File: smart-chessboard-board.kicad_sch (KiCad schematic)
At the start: 5 parts, among them J101 Conn_01x12_MountingPin

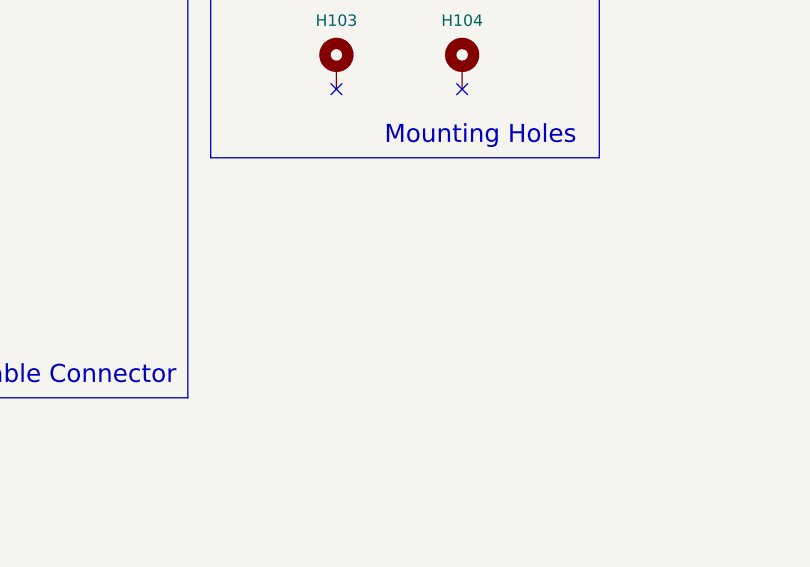
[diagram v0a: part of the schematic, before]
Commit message: complete trace and add test points
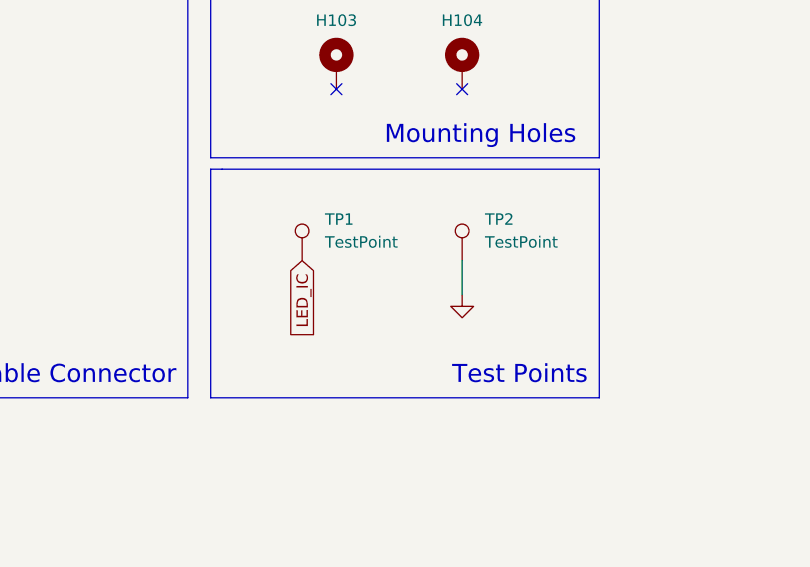
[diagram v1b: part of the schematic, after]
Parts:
- added TP1, TP2: TestPoint, TestPoint:TestPoint_Pad_D2.0mm, symbol Connector:TestPoint
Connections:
- net GND: now also TP2.1
- net LED_IC: now also TP1.1
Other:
- note added: "Test Points"
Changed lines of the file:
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@@
+    (stroke (width 0) (type default) (color 0 0 0 0))
+  )
+  (polyline (pts (xy 100.33 54.61) (xy 101.6 54.61))
     (stroke (width 0) (type default) (color 0 0 0 0))
   )
@@
     (stroke (width 0) (type default) (color 0 0 0 0))
   )
+  (wire (pts (xy 128.27 68.58) (xy 128.27 64.77))
+    (stroke (width 0) (type default) (color 0 0 0 0))
+  )
   (polyline (pts (xy 21.59 20.32) (xy 97.79 20.32))
     (stroke (width 0) (type default) (color 0 0 0 0))
@@
     (stroke (width 0) (type default) (color 0 0 0 0))
   )
+  (polyline (pts (xy 101.6 54.61) (xy 143.51 54.61))
+    (stroke (width 0) (type default) (color 0 0 0 0))
+  )
   (polyline (pts (xy 143.51 20.32) (xy 143.51 53.34))
     (stroke (width 0) (type default) (color 0 0 0 0))
   )
+  (polyline (pts (xy 100.33 80.01) (xy 100.33 54.61))
+    (stroke (width 0) (type default) (color 0 0 0 0))
+  )
   (polyline (pts (xy 97.79 20.32) (xy 97.79 80.01))
     (stroke (width 0) (type default) (color 0 0 0 0))
@@
     (stroke (width 0) (type default) (color 0 0 0 0))
   )
+  (polyline (pts (xy 143.51 80.01) (xy 100.33 80.01))
+    (stroke (width 0) (type default) (color 0 0 0 0))
+  )
   (wire (pts (xy 35.56 38.1) (xy 35.56 40.64))
     (stroke (width 0) (type default) (color 0 0 0 0))
   )
   (wire (pts (xy 57.15 38.1) (xy 38.1 38.1))
+    (stroke (width 0) (type default) (color 0 0 0 0))
+  )
+  (polyline (pts (xy 143.51 54.61) (xy 143.51 80.01))
     (stroke (width 0) (type default) (color 0 0 0 0))
   )
@@
   )
   (text "Flexible Flat Cable Connector" (at 96.52 78.74 180)
+    (effects (font (size 2 2)) (justify right bottom))
+  )
+  (text "Test Points" (at 142.24 78.74 180)
     (effects (font (size 2 2)) (justify right bottom))
   )
@@
     )
   )
+  (global_label "LED_IC" (shape input) (at 110.49 64.77 270) (fields_autoplaced)
+    (effects (font (size 1.27 1.27)) (justify right))
+    (property "Intersheet References" "${INTERSHEET_REFS}" (id 0) (at 110.4106 73.4726 90)
+      (effects (font (size 1.27 1.27)) (justify right) hide)
+    )
+  )
   (global_label "~{IO_INT0}" (shape output) (at 49.53 53.34 180) (fields_autoplaced)
     (effects (font (size 1 1)) (justify right))
@@
     (pin "1")
   )
+  (symbol (lib_id "Connector:TestPoint") (at 110.49 64.77 0) (unit 1)
+    (in_bom yes) (on_board yes) (fields_autoplaced)
+    (property "Reference" "TP1" (id 0) (at 113.03 60.1979 0)
+      (effects (font (size 1.27 1.27)) (justify left))
+    )
+    (property "Value" "TestPoint" (id 1) (at 113.03 62.7379 0)
+      (effects (font (size 1.27 1.27)) (justify left))
+    )
+    (property "Footprint" "TestPoint:TestPoint_Pad_D2.0mm" (id 2) (at 115.57 64.77 0)
+      (effects (font (size 1.27 1.27)) hide)
+    )
+    (property "Datasheet" "~" (id 3) (at 115.57 64.77 0)
+      (effects (font (size 1.27 1.27)) hide)
+    )
+    (pin "1")
+  )
   (symbol (lib_id "Mechanical:MountingHole_Pad") (at 114.3 30.48 0) (unit 1)
     (in_bom yes) (on_board yes)
@@
     (pin "1")
   )
+  (symbol (lib_id "Connector:TestPoint") (at 128.27 64.77 0) (unit 1)
+    (in_bom yes) (on_board yes)
+    (property "Reference" "TP2" (id 0) (at 130.81 60.1979 0)
+      (effects (font (size 1.27 1.27)) (justify left))
+    )
+    (property "Value" "TestPoint" (id 1) (at 130.81 62.7379 0)
+      (effects (font (size 1.27 1.27)) (justify left))
+    )
+    (property "Footprint" "TestPoint:TestPoint_Pad_D2.0mm" (id 2) (at 133.35 64.77 0)
+      (effects (font (size 1.27 1.27)) hide)
+    )
+    (property "Datasheet" "~" (id 3) (at 133.35 64.77 0)
+      (effects (font (size 1.27 1.27)) hide)
+    )
+    (pin "1")
+  )
   (symbol (lib_id "Mechanical:MountingHole_Pad") (at 128.27 43.18 0) (unit 1)
     (in_bom yes) (on_board yes)
@@
     )
     (property "Datasheet" "~" (id 3) (at 55.88 30.48 0)
+      (effects (font (size 1.27 1.27)) hide)
+    )
+    (pin "1")
+  )
+  (symbol (lib_id "power:GND") (at 128.27 68.58 0) (unit 1)
+    (in_bom yes) (on_board yes) (fields_autoplaced)
+    (property "Reference" "#PWR0102" (id 0) (at 128.27 74.93 0)
+      (effects (font (size 1.27 1.27)) hide)
+    )
+    (property "Value" "GND" (id 1) (at 128.27 73.66 0)
+      (effects (font (size 1.27 1.27)) hide)
+    )
+    (property "Footprint" "" (id 2) (at 128.27 68.58 0)
+      (effects (font (size 1.27 1.27)) hide)
+    )
+    (property "Datasheet" "" (id 3) (at 128.27 68.58 0)
       (effects (font (size 1.27 1.27)) hide)
     )
@@
       (reference "#PWR0101") (unit 1) (value "GND") (footprint "")
     )
+    (path "/55274c2f-dbb8-49a9-b7eb-36ea01e536da"
+      (reference "#PWR0102") (unit 1) (value "GND") (footprint "")
+    )
     (path "/66c9bcf1-b54f-4dc7-a010-91aca42cde15/8f22366e-865e-43b5-9b26-7063286fd7bd"
       (reference "#PWR0201") (unit 1) (value "GND") (footprint "")
@@
       (reference "R464") (unit 1) (value "2K7") (footprint "Resistor_SMD:R_0603_1608Metric")
     )
+    (path "/1170309c-d754-4a50-aa7d-8845703787a4"
+      (reference "TP1") (unit 1) (value "TestPoint") (footprint "TestPoint:TestPoint_Pad_D2.0mm")
+    )
+    (path "/346543ee-2396-45d4-88dd-56f70b824909"
+      (reference "TP2") (unit 1) (value "TestPoint") (footprint "TestPoint:TestPoint_Pad_D2.0mm")
+    )
     (path "/c4f5f719-807b-479b-9073-cc19a7c7c375/b4d31827-41e5-4a00-9f89-3655a40f3d7f"
